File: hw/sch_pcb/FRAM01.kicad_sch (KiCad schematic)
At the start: 9 parts, among them IC1 CY15B108QN-40SXI, J2 HEADER_2x04, M1 HOLE M3, M2 HOLE M3, M3 HOLE, M4 HOLE

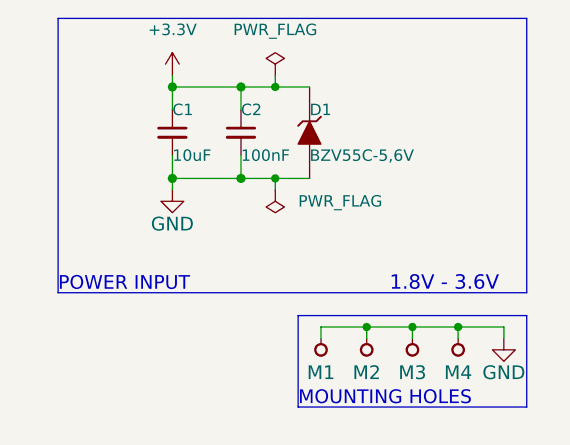
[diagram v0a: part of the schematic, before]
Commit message: change zener diode, minor improvements in silkscreen
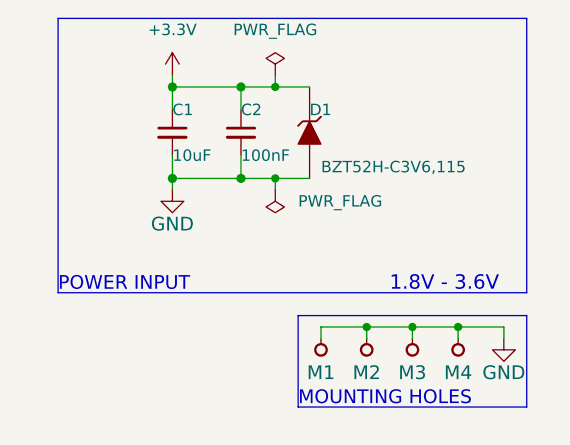
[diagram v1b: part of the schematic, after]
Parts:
- D1: value BZV55C-5,6V -> BZT52H-C3V6,115; footprint Diode_SMD:D_SMA -> Diode_SMD:D_SOD-123F; UST_ID 5c70984512875079b91f88b2 -> (none)

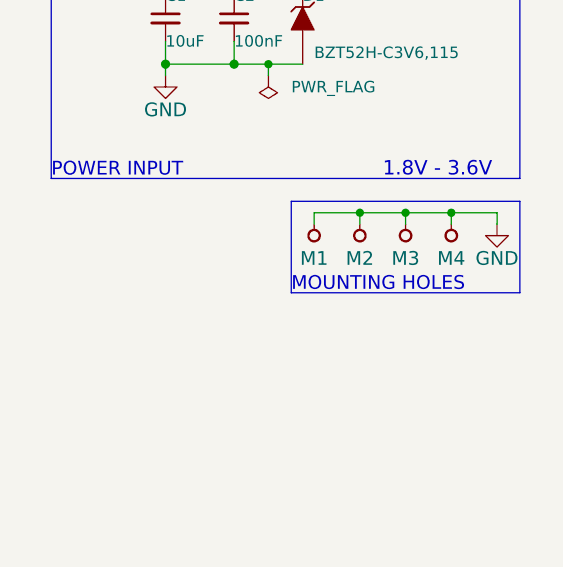
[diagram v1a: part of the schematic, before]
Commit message: add fiducial
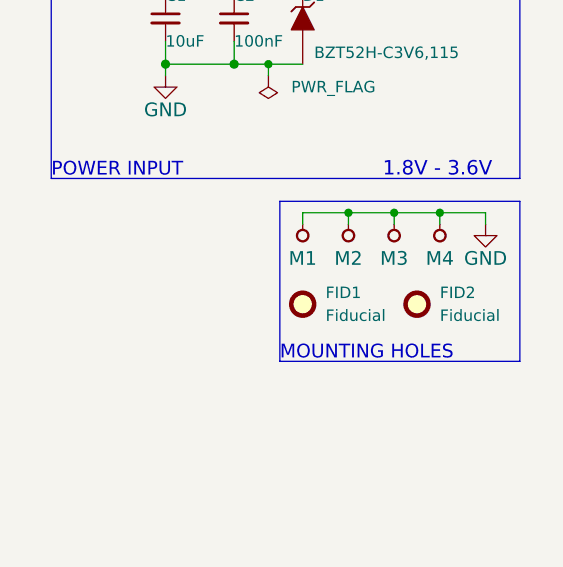
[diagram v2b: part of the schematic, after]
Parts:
- added FID1, FID2: Fiducial, Fiducial:Fiducial_1mm_Mask2mm, symbol Mechanical:Fiducial
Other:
- moved on the sheet: M1, M2, M3, M4

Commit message: Split silkscreen to avoid collision with vias. Update title-block
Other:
- company: (none) -> MLAB.cz
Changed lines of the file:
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@@
     (title "FRAM01A")
     (date "2023-06-09")
+    (company "MLAB.cz")
+    (comment 1 "FRAM based data storage")
   )
   (junction (at 210.82 95.25) (diameter 0) (color 0 0 0 0)

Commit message: power connection added, SPI connector changed, cherrypick, simple repairs
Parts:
- added J1: HEADER_2x03_PARALLEL, Connector_PinHeader_2.54mm:PinHeader_2x03_P2.54mm_Vertical, symbol MLAB_HEADER:HEADER_2x03_PARALLEL
- FID1, FID2, M1, M2, M3, M4: now left out of the parts list
- J2: footprint Mlab_Pin_Headers:Straight_2x04 -> Connector_PinHeader_2.54mm:PinHeader_2x04_P2.54mm_Vertical
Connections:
- net +3.3V: now also J1.3, J1.4
- net GND: now also J1.1, J1.2, J1.5, J1.6
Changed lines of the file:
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@@
   (junction (at 266.7 52.07) (diameter 0) (color 0 0 0 0)
   )
+  (junction (at 193.04 68.58) (diameter 0) (color 0 0 0 0)
+  )
   (junction (at 241.3 35.56) (diameter 1.016) (color 0 0 0 0)
   )
@@
   )
   (no_connect (at 153.67 88.9))
+  (wire (pts (xy 193.04 68.58) (xy 195.58 68.58))
+    (stroke (width 0) (type default))
+  )
   (wire (pts (xy 261.62 52.07) (xy 256.54 52.07))
     (stroke (width 0) (type default))
@@
     (stroke (width 0) (type default))
   )
+  (wire (pts (xy 190.5 66.04) (xy 195.58 66.04))
+    (stroke (width 0) (type default))
+  )
   (polyline (pts (xy 280.67 68.58) (xy 254 68.58))
     (stroke (width 0) (type default))
@@
     (stroke (width 0) (type solid))
   )
+  (wire (pts (xy 193.04 63.5) (xy 193.04 68.58))
+    (stroke (width 0) (type default))
+  )
   (wire (pts (xy 276.86 53.34) (xy 276.86 52.07))
     (stroke (width 0) (type default))
@@
     (stroke (width 0) (type default))
   )
+  (wire (pts (xy 195.58 63.5) (xy 193.04 63.5))
+    (stroke (width 0) (type default))
+  )
   (polyline (pts (xy 228.6 48.26) (xy 280.67 48.26))
     (stroke (width 0) (type default))
@@
   )
   (wire (pts (xy 252.73 24.13) (xy 252.73 25.4))
+    (stroke (width 0) (type default))
+  )
+  (wire (pts (xy 193.04 68.58) (xy 193.04 71.12))
     (stroke (width 0) (type default))
   )
@@
   )
   (symbol (lib_id "power:PWR_FLAG") (at 252.73 24.13 0) (unit 1)
-    (in_bom yes) (on_board yes) (dnp no) (fields_autoplaced)
+    (in_bom no) (on_board yes) (dnp no) (fields_autoplaced)
     (property "Reference" "#FLG01" (at 252.73 22.225 0)
       (effects (font (size 1.27 1.27)) hide)
@@
   )
   (symbol (lib_id "power:PWR_FLAG") (at 252.73 36.83 180) (unit 1)
-    (in_bom yes) (on_board yes) (dnp no) (fields_autoplaced)
+    (in_bom no) (on_board yes) (dnp no) (fields_autoplaced)
     (property "Reference" "#FLG02" (at 252.73 38.735 0)
       (effects (font (size 1.27 1.27)) hide)
@@
   )
   (symbol (lib_id "mlab-default-rescue:HOLE") (at 256.54 54.61 90) (unit 1)
-    (in_bom yes) (on_board yes) (dnp no)
+    (in_bom no) (on_board yes) (dnp no)
     (property "Reference" "M1" (at 256.54 57.15 90)
       (effects (font (size 1.524 1.524)))
@@
     )
   )
+  (symbol (lib_id "MLAB_HEADER:HEADER_2x03_PARALLEL") (at 201.93 66.04 0) (unit 1)
+    (in_bom yes) (on_board yes) (dnp no) (fields_autoplaced)
+    (property "Reference" "J1" (at 205.74 66.04 0)
+      (effects (font (size 1.524 1.524)) (justify left))
+    )
+    (property "Value" "HEADER_2x03_PARALLEL" (at 205.74 67.31 0)
+      (effects (font (size 1.524 1.524)) (justify left) hide)
+    )
+    (property "Footprint" "Connector_PinHeader_2.54mm:PinHeader_2x03_P2.54mm_Vertical" (at 201.93 63.5 0)
+      (effects (font (size 1.524 1.524)) hide)
+    )
+    (property "Datasheet" "" (at 201.93 63.5 0)
+      (effects (font (size 1.524 1.524)))
+    )
+    (pin "1")
+    (pin "2")
+    (pin "3")
+    (pin "4")
+    (pin "5")
+    (pin "6")
+    (instances
+      (project "FRAM01"
+        (path "/94090ec1-0e6b-403a-88b7-50640bad6d28"
+          (reference "J1") (unit 1)
+        )
+      )
+    )
+  )
   (symbol (lib_id "Mechanical:Fiducial") (at 269.24 62.23 0) (unit 1)
-    (in_bom yes) (on_board yes) (dnp no) (fields_autoplaced)
+    (in_bom no) (on_board yes) (dnp no) (fields_autoplaced)
     (property "Reference" "FID2" (at 271.78 60.96 0)
       (effects (font (size 1.27 1.27)) (justify left))
@@
   )
   (symbol (lib_id "mlab-default-rescue:HOLE") (at 266.7 54.61 90) (unit 1)
-    (in_bom yes) (on_board yes) (dnp no)
+    (in_bom no) (on_board yes) (dnp no)
     (property "Reference" "M3" (at 266.7 57.15 90)
       (effects (font (size 1.524 1.524)))
@@
   )
   (symbol (lib_id "mlab-default-rescue:HOLE") (at 271.78 54.61 90) (unit 1)
-    (in_bom yes) (on_board yes) (dnp no)
+    (in_bom no) (on_board yes) (dnp no)
     (property "Reference" "M4" (at 271.78 57.15 90)
       (effects (font (size 1.524 1.524)))
@@
     )
   )
+  (symbol (lib_name "GND_1") (lib_id "power:GND") (at 193.04 71.12 0) (unit 1)
+    (in_bom yes) (on_board yes) (dnp no) (fields_autoplaced)
+    (property "Reference" "#PWR06" (at 193.04 77.47 0)
+      (effects (font (size 1.27 1.27)) hide)
+    )
+    (property "Value" "GND" (at 193.04 76.2 0)
+      (effects (font (size 1.27 1.27)))
+    )
+    (property "Footprint" "" (at 193.04 71.12 0)
+      (effects (font (size 1.27 1.27)) hide)
+    )
+    (property "Datasheet" "" (at 193.04 71.12 0)
+      (effects (font (size 1.27 1.27)) hide)
+    )
+    (pin "1")
+    (instances
+      (project "FRAM01"
+        (path "/94090ec1-0e6b-403a-88b7-50640bad6d28"
+          (reference "#PWR06") (unit 1)
+        )
+      )
+    )
+  )
   (symbol (lib_id "mlab-default-rescue:HOLE") (at 261.62 54.61 90) (unit 1)
-    (in_bom yes) (on_board yes) (dnp no)
+    (in_bom no) (on_board yes) (dnp no)
     (property "Reference" "M2" (at 261.62 57.15 90)
       (effects (font (size 1.524 1.524)))
@@
   )
   (symbol (lib_id "Mechanical:Fiducial") (at 256.54 62.23 0) (unit 1)
-    (in_bom yes) (on_board yes) (dnp no) (fields_autoplaced)
+    (in_bom no) (on_board yes) (dnp no) (fields_autoplaced)
     (property "Reference" "FID1" (at 259.08 60.96 0)
       (effects (font (size 1.27 1.27)) (justify left))
@@
       (effects (font (size 1.524 1.524)) hide)
     )
-    (property "Footprint" "Mlab_Pin_Headers:Straight_2x04" (at 203.2 87.63 0)
+    (property "Footprint" "Connector_PinHeader_2.54mm:PinHeader_2x04_P2.54mm_Vertical" (at 203.2 87.63 0)
       (effects (font (size 1.524 1.524)) hide)
     )
@@
         )
       )
+    )
+  )
+  (symbol (lib_id "power:+3.3V") (at 190.5 66.04 0) (unit 1)
+    (in_bom yes) (on_board yes) (dnp no) (fields_autoplaced)
+    (property "Reference" "#PWR08" (at 190.5 69.85 0)
+      (effects (font (size 1.27 1.27)) hide)
+    )
+    (property "Value" "+3.3V" (at 190.5 60.96 0)
+      (effects (font (size 1.27 1.27)))
+    )
+    (property "Footprint" "" (at 190.5 66.04 0)
+      (effects (font (size 1.27 1.27)) hide)
+    )
+    (property "Datasheet" "" (at 190.5 66.04 0)
+      (effects (font (size 1.27 1.27)) hide)
+    )
+    (pin "1")
+    (instances
+      (project "FRAM01"
+        (path "/94090ec1-0e6b-403a-88b7-50640bad6d28"
+          (reference "#PWR08") (unit 1)
+        )
+      )

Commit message: add ustid
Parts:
- D1: UST_ID (none) -> 650b35ab462c6d9e720543d0
- IC1: UST_ID (none) -> 650b3dae462c6d9e72054477
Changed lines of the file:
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@@
       (effects (font (size 1.524 1.524)) hide)
     )
-    (property "UST_ID" "" (at 256.54 30.48 0)
+    (property "UST_ID" "650b35ab462c6d9e720543d0" (at 256.54 30.48 0)
       (effects (font (size 1.27 1.27)) hide)
     )
@@
       (effects (font (size 1.27 1.27)) (justify left) hide)
     )
+    (property "UST_ID" "650b3dae462c6d9e72054477" (at 128.27 86.36 0)
+      (effects (font (size 1.27 1.27)) hide)
+    )
     (pin "1")

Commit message: fram layout
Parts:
- C2: UST_ID 5c70984812875079b91f8bf2 -> 5c70984712875079b91f8b4c
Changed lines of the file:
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@@
       (effects (font (size 1.27 1.27)) hide)
     )
-    (property "UST_ID" "5c70984812875079b91f8bf2" (at -1.27 59.69 0)
+    (property "UST_ID" "5c70984712875079b91f8b4c" (at -1.27 59.69 0)
       (effects (font (size 1.27 1.27)) hide)
     )
